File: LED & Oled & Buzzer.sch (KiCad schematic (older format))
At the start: 20 parts, among them J6 A1250WV-S-4P, Q4 BC847

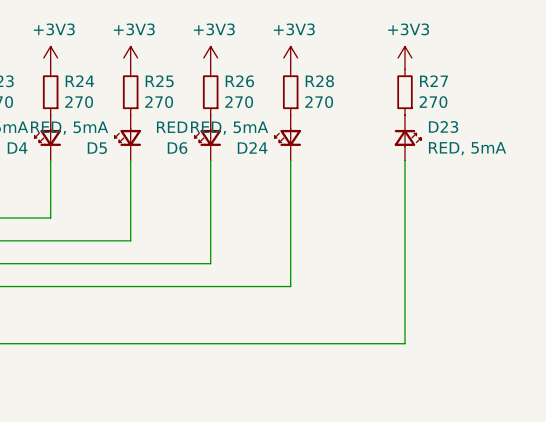
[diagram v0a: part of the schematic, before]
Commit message: Flip led, fix path
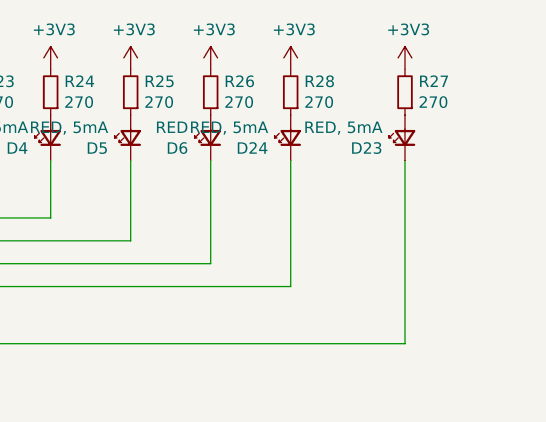
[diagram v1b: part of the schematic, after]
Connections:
- net ~LED_MOUSE_EYE: now also D23.1 (K); no longer D23.2 (A)
- net at R27.1: now also D23.2 (A); no longer D23.1 (K)
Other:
- moved on the sheet: D23
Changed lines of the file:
@@
 F 3 "~" V 8900 1700 50  0001 C CNN
 	1    8900 1700
-	0    1    1    0
+	0    -1   -1   0
 $EndComp
 Wire Wire Line

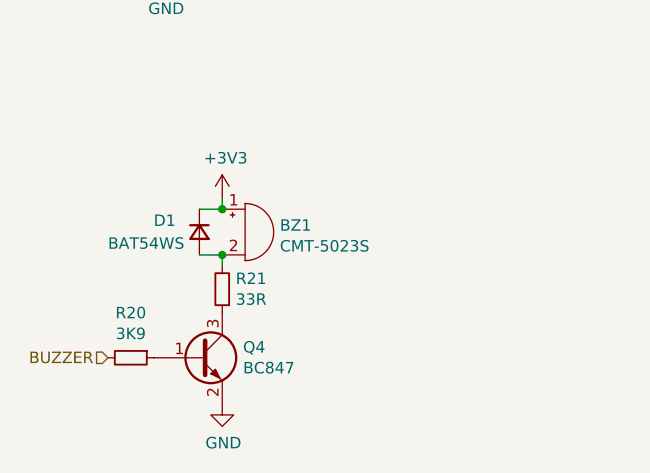
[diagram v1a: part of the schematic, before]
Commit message: Usunięto rezystor przy buzzerze, poprawiono połączenia do WS2812B
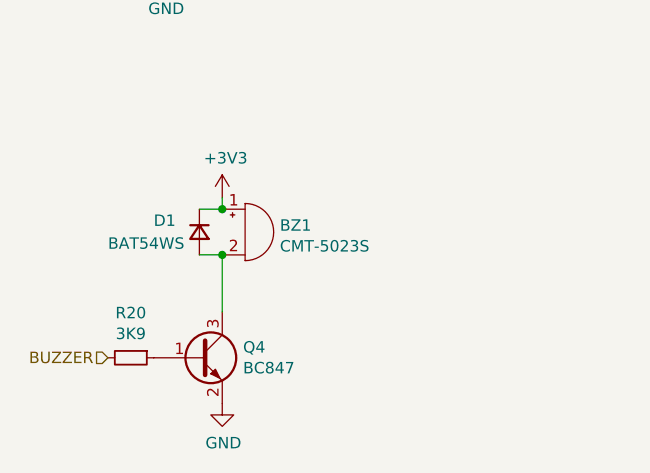
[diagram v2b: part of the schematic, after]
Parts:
- removed R21: 33R, Resistor_SMD:R_0402_1005Metric, symbol Device:R_Small
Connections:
- net at BZ1.2 (+), D1.2 (A): now also Q4.3 (C)
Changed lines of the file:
@@
-$EndComp
-$Comp
-L Device:R_Small R21
-U 1 1 5E6B67DA
-P 3600 4050
-F 0 "R21" H 3541 4004 50  0000 R CNN
-F 1 "33R" H 3541 4095 50  0000 R CNN
-F 2 "Resistor_SMD:R_0402_1005Metric" H 3600 4050 50  0001 C CNN
-F 3 "~" H 3600 4050 50  0001 C CNN
-	1    3600 4050
-	-1   0    0    1
 $EndComp
 $Comp
@@
 ~LED_5
 Wire Wire Line
-	3600 3950 3600 3900
-Wire Wire Line
 	3600 3700 3600 3650
 $Comp
@@
 Text HLabel 6400 2350 0    50   Input ~ 0
 ~LED_6
+Wire Wire Line
+	3600 3900 3600 4150
 $EndSCHEMATC
